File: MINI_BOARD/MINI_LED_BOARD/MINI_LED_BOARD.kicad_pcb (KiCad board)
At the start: 2 copper layers, 65.8 x 6 mm, 44 parts, among them J1 Conn_ARM_SWD_TagConnect_TC2030, J2 430450428, U1 MSPM0C1103SDDFR, U2 TCAN334, U4 TPS76333DBVR

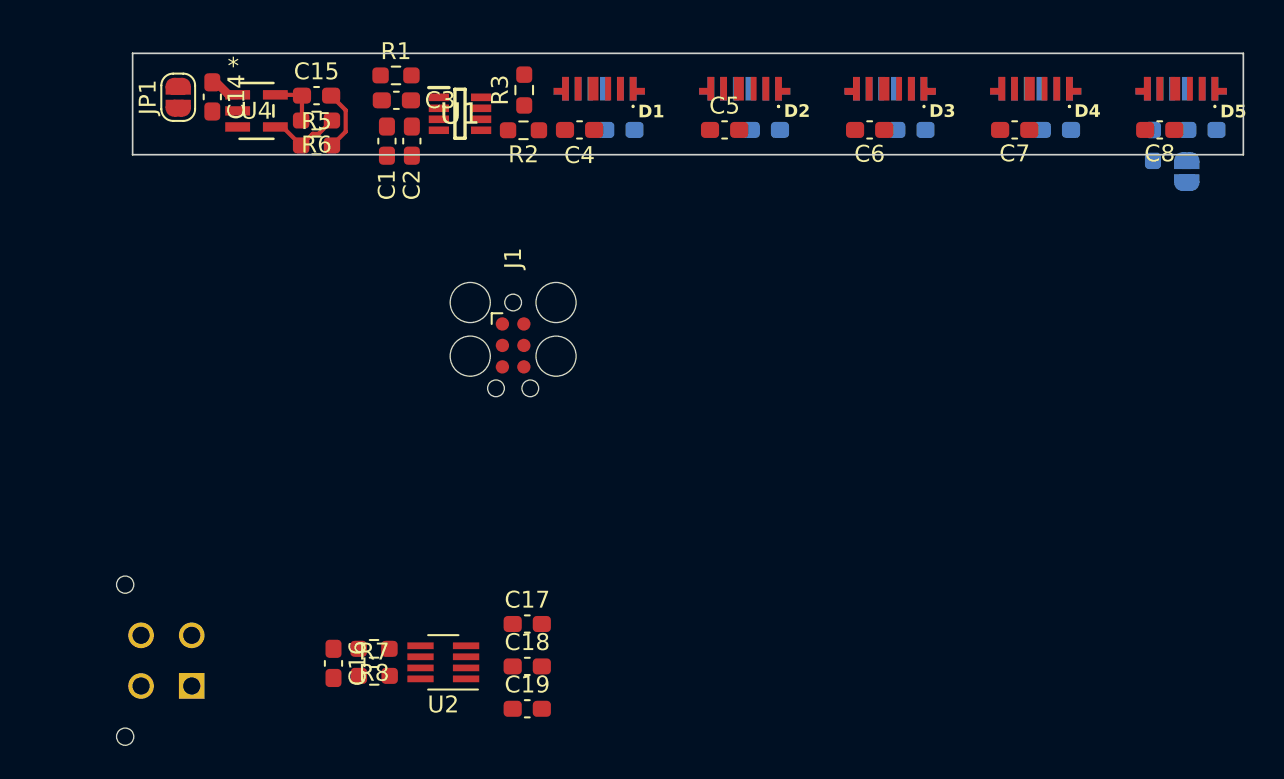
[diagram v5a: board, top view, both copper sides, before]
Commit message: Refine board shape and layout
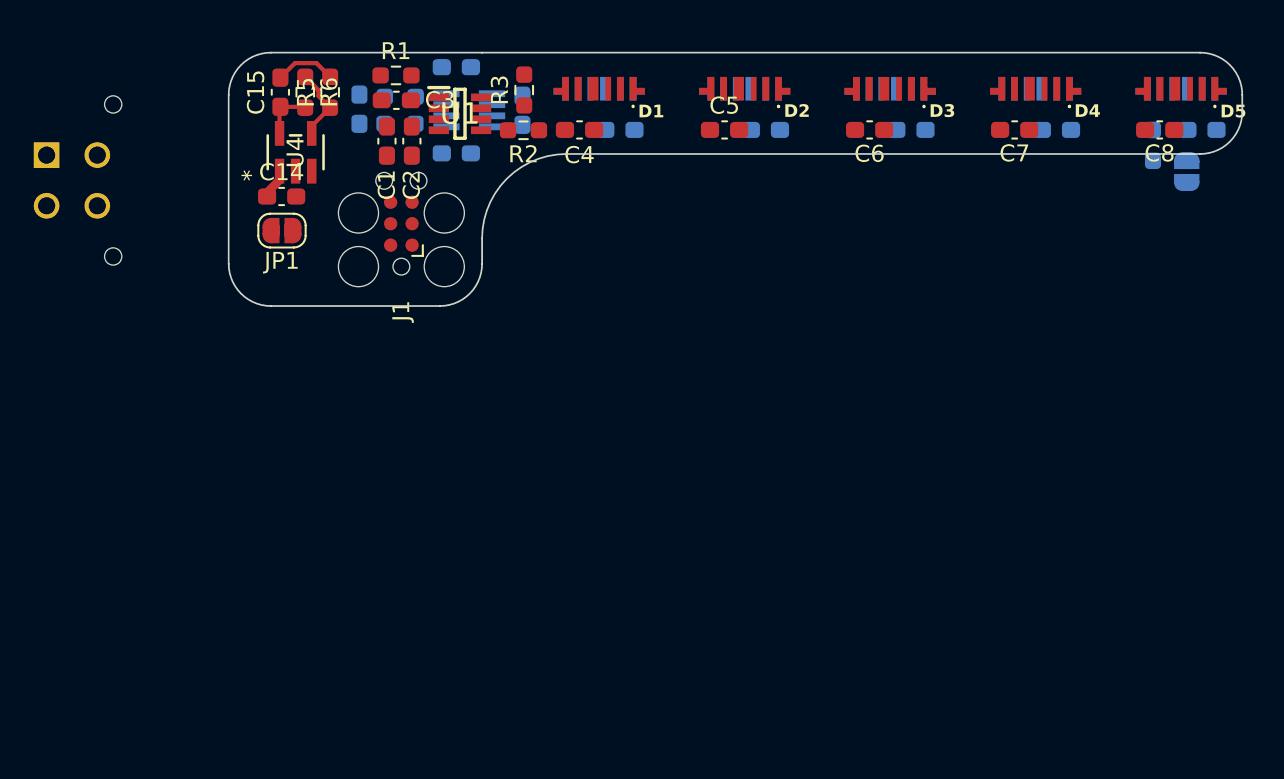
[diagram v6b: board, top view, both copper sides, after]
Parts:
- C16, C17, C18, C19, R7, R8, U2: moved to B.Cu
- moved C18 35.7 mm to (74.2, 54.0)
- moved R7 34.3 mm to (70.8, 55.7)
- moved C19 33.1 mm to (74.2, 59.1)
- moved C16 32.8 mm to (68.4, 56.5), turned to 90 degrees
- moved U2 32.7 mm to (74.9, 56.5)
- moved J2 32.6 mm to (49.9, 59.2), turned to 90 degrees
- moved R8 31.1 mm to (70.8, 57.3)
- moved C17 30.4 mm to (78.1, 56.5), turned to -90 degrees
- moved JP1 10.0 mm to (63.8, 63.6), turned to 180 degrees
- moved J1 9.78 mm to (70.9, 63.2), turned to 90 degrees
- moved C14 7.18 mm to (63.8, 61.6), turned to 0 degrees
- moved U4 3.37 mm to (64.6, 59.0), turned to 90 degrees
- moved R5 3.25 mm to (66.7, 55.5), turned to 90 degrees
- moved C15 2.15 mm to (63.7, 55.5), turned to 90 degrees
- moved R6 1.80 mm to (65.2, 55.5), turned to -90 degrees
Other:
- board size 65.8 x 6 mm -> 60 x 15 mm

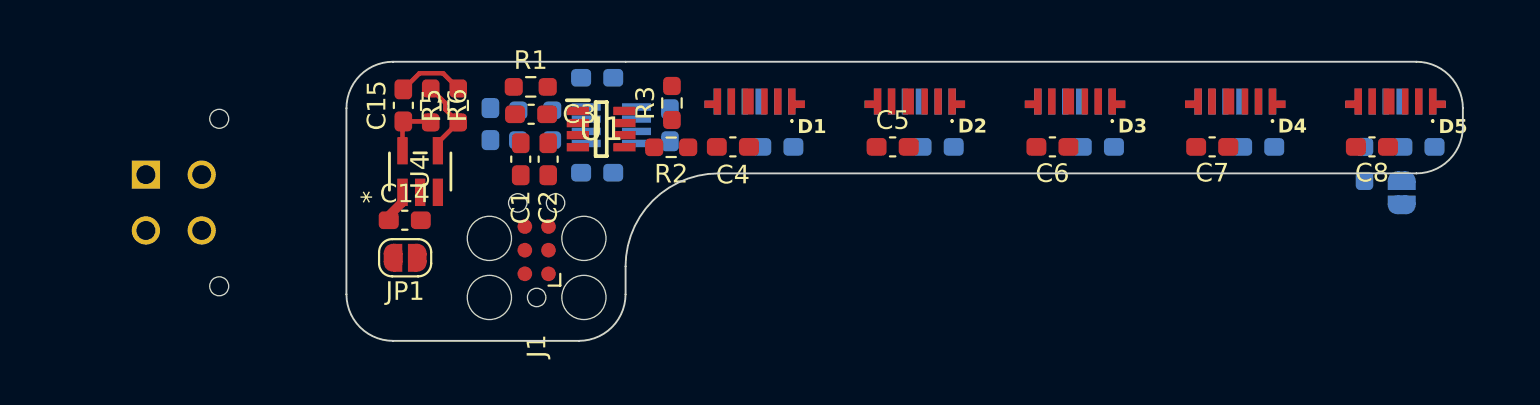
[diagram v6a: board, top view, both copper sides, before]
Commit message: Finalize layout and conenction features; begin routing
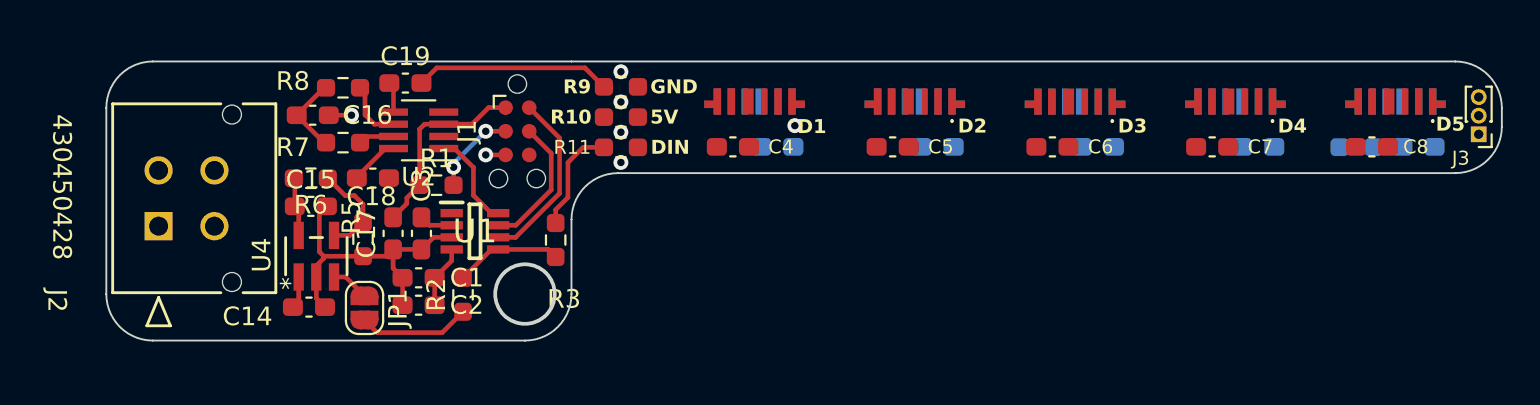
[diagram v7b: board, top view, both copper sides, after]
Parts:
- removed JP2: SolderJumper_2_Open, Jumper:SolderJumper-2_P1.3mm_Open_RoundedPad1.0x1.5mm
- added J3: Conn_01x03_Socket, Connector_PinHeader_1.00mm:PinHeader_1x03_P1.00mm_Vertical, F.Cu at (121.5, 57.0)
- added R10: 0, Resistor_SMD:R_0603_1608Metric_Pad0.98x0.95mm_HandSolder, F.Cu at (75.4, 56.1)
- added R11: 0, Resistor_SMD:R_0603_1608Metric_Pad0.98x0.95mm_HandSolder, F.Cu at (75.4, 57.7)
- added R9: 0, Resistor_SMD:R_0603_1608Metric_Pad0.98x0.95mm_HandSolder, F.Cu at (75.4, 54.5)
- C16, C17, C18, C19, J2, R7, R8, U2: moved to F.Cu
- J1: value Conn_ARM_SWD_TagConnect_TC2030 -> Conn_ARM_SWD_TagConnect_TC2030-NL; footprint Connector:Tag-Connect_TC2030-IDC-FP_2x03_P1.27mm_Vertical -> Connector:Tag-Connect_TC2030-IDC-NL_2x03_P1.27mm_Vertical
- moved C17 16.0 mm to (63.2, 62.3), turned to 90 degrees
- moved R2 13.7 mm to (67.0, 65.6), turned to 90 degrees
- moved C18 13.2 mm to (62.1, 59.4)
- moved C19 11.4 mm to (63.9, 54.3)
- moved R8 10.7 mm to (60.5, 54.5)
- moved C2 10.5 mm to (64.6, 66.2), turned to 180 degrees
- moved R7 10.5 mm to (60.5, 57.5)
- moved U2 10.4 mm to (64.6, 56.8)
- moved R3 9.66 mm to (71.9, 62.7)
- moved C16 9.56 mm to (58.9, 56.0), turned to 0 degrees
- moved R5 8.82 mm to (61.6, 62.6), turned to -90 degrees
- moved U1 8.73 mm to (67.6, 62.2)
- moved C3 8.70 mm to (64.7, 62.3), turned to -90 degrees
- moved C1 8.41 mm to (64.6, 64.7), turned to 180 degrees
- moved R6 7.54 mm to (58.8, 59.4), turned to 180 degrees
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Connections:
- C10 pad 1: +5V -> VDD
- C10 pad 2: GND -> GND2
- C11 pad 1: +5V -> VDD
- C11 pad 2: GND -> GND2
- C12 pad 1: +5V -> VDD
- C12 pad 2: GND -> GND2
- C13 pad 1: +5V -> VDD
- C13 pad 2: GND -> GND2
- C4 pad 1: +5V -> VDD
- C4 pad 2: GND -> GND2
- C5 pad 1: +5V -> VDD
- C5 pad 2: GND -> GND2
- C6 pad 1: +5V -> VDD
- C6 pad 2: GND -> GND2
- C7 pad 1: +5V -> VDD
- C7 pad 2: GND -> GND2
- C8 pad 1: +5V -> VDD
- C8 pad 2: GND -> GND2
- C9 pad 1: +5V -> VDD
- C9 pad 2: GND -> GND2
- D1 pad 1: +5V -> VDD
- D1 pad 4: GND -> GND2
- D1 pad 5: +5V -> VDD
- D10 pad 1: +5V -> VDD
- D10 pad 4: GND -> GND2
- D10 pad 5: +5V -> VDD
- D2 pad 1: +5V -> VDD
- D2 pad 4: GND -> GND2
- D2 pad 5: +5V -> VDD
- D3 pad 1: +5V -> VDD
- D3 pad 4: GND -> GND2
- D3 pad 5: +5V -> VDD
- D4 pad 1: +5V -> VDD
- D4 pad 4: GND -> GND2
- D4 pad 5: +5V -> VDD
- D5 pad 1: +5V -> VDD
- D5 pad 4: GND -> GND2
- D5 pad 5: +5V -> VDD
- D6 pad 1: +5V -> VDD
- D6 pad 4: GND -> GND2
- D6 pad 5: +5V -> VDD
- D7 pad 1: +5V -> VDD
- D7 pad 4: GND -> GND2
- D7 pad 5: +5V -> VDD
- D8 pad 1: +5V -> VDD
- D8 pad 4: GND -> GND2
- D8 pad 5: +5V -> VDD
- D9 pad 1: +5V -> VDD
- D9 pad 4: GND -> GND2
- D9 pad 5: +5V -> VDD
- J2 pad 1: +5V -> GND
- J2 pad 2: Net-(U2-CANH) -> +5V
- J2 pad 4: GND -> Net-(U2-CANH)
- R3 pad 2: Net-(D1-DIN) -> Net-(R11-Pad2)
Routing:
- net GND: track 3.64 -> 29.6 mm, vias 0 -> 2
- net +3.3V: track 3.09 -> 17.0 mm
- net Net-(J1-SWDIO): track 0.00 -> 9.56 mm
- net Net-(J1-SWCLK): track 0.00 -> 7.27 mm
- net Net-(J1-~{RESET}): track 0.00 -> 6.48 mm, vias 0 -> 2
- net +5V: track 1.81 -> 7.79 mm
- net Net-(R11-Pad2): track 0.00 -> 5.80 mm
- net Net-(U1-PA0): track 0.00 -> 5.78 mm
- net Net-(U1-PA24_/_A3/UART_RX): track 0.00 -> 5.24 mm
- net Net-(C16-Pad1): track 0.00 -> 4.37 mm
- net Net-(U2-CANL): track 0.00 -> 3.36 mm
- net Net-(U2-STB): track 0.00 -> 2.66 mm
- net Net-(JP1-A): track 0.00 -> 2.06 mm
- net Net-(U2-CANH): track 0.00 -> 1.94 mm
- net Net-(U2-SHDN): track 0.00 -> 1.65 mm
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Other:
- board size 60 x 15 mm -> 75 x 15 mm
- board text added: "5V"
- board text added: "DIN"
- board text added: "GND"
